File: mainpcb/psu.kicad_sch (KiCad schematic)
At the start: 16 parts, among them J2 8PCV-06-006, U3 LM2576T-5

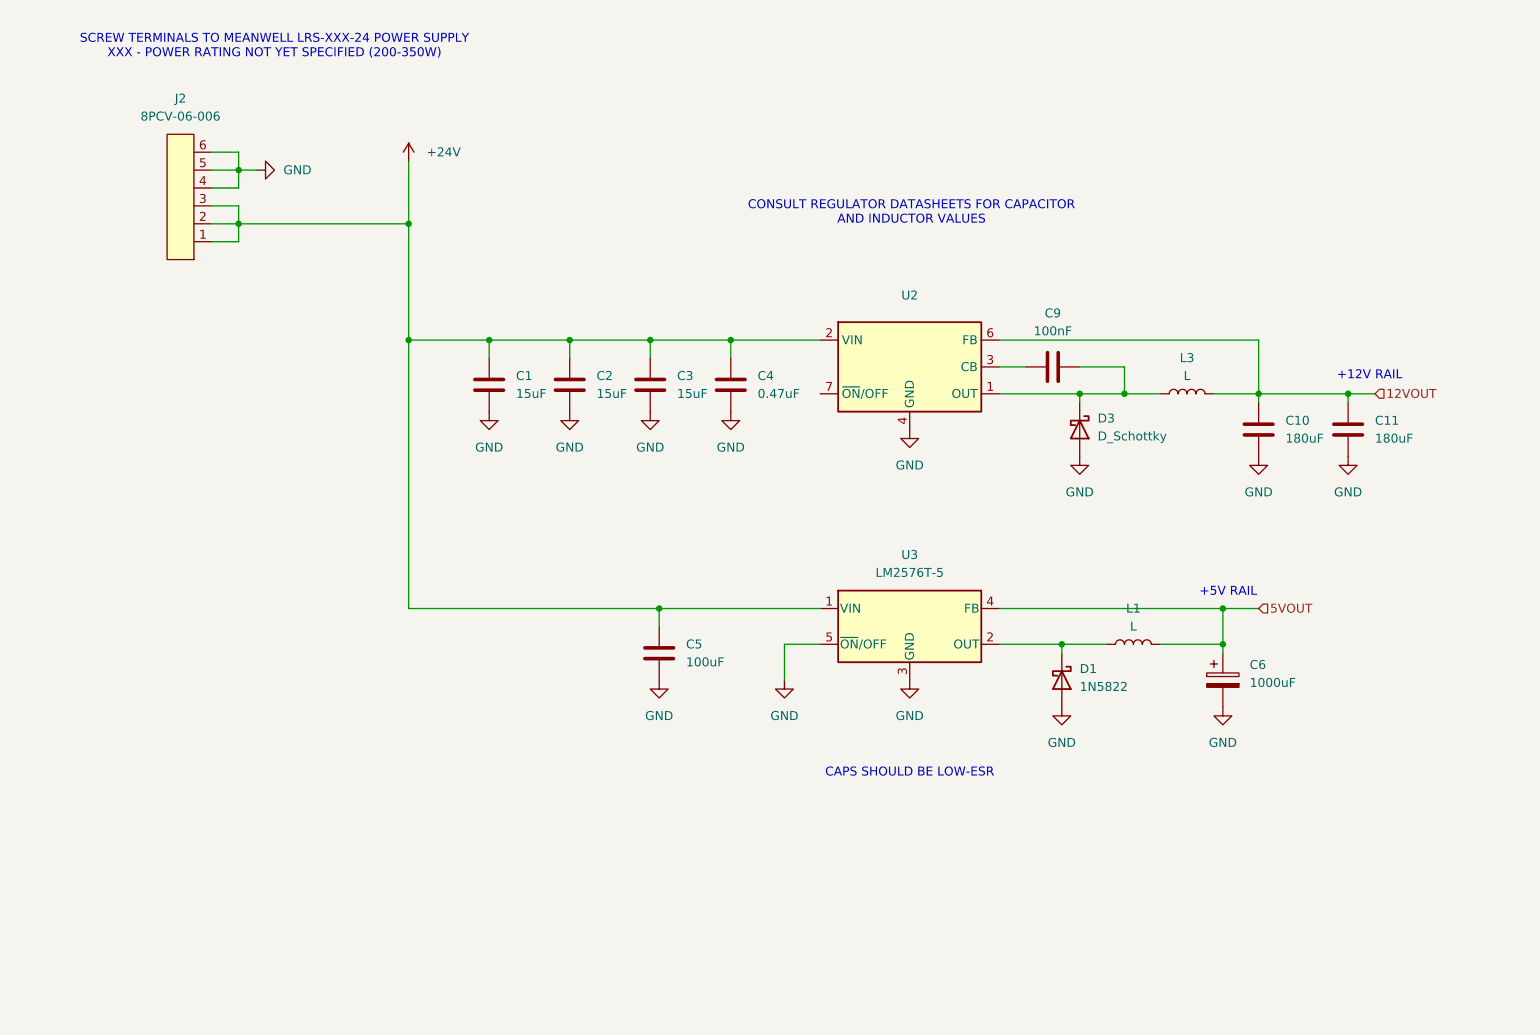
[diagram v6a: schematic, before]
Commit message: Added limit switches to hand and readme
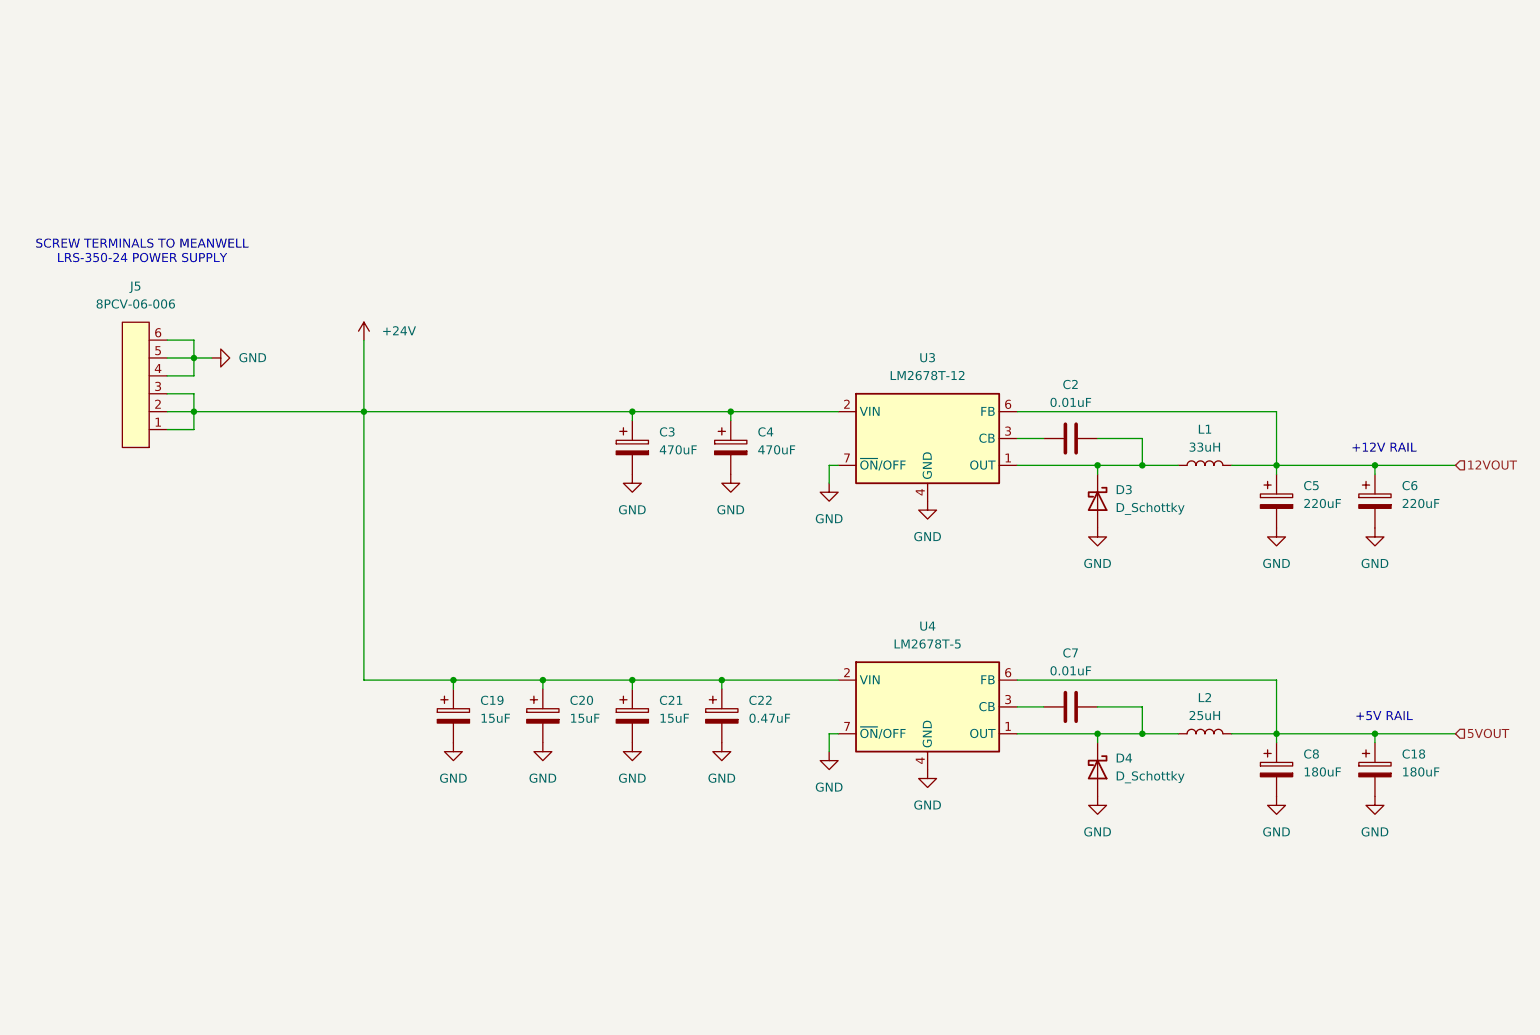
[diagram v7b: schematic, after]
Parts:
- removed C1, C2, C3: 15uF, symbol Device:C
- removed C10, C11: 180uF, symbol Device:C
- removed C4: 0.47uF, symbol Device:C
- removed C5: 100uF, symbol Device:C
- removed D1: 1N5822, symbol Device:D_Schottky
- removed L1: L, symbol Device:L
- removed U2: ~, symbol bh_symbol_library:LM2678T-12
- removed U3: LM2576T-5, Package_TO_SOT_THT:TO-220-5_P3.4x3.7mm_StaggerOdd_Lead3.8mm_Vertical, symbol Regulator_Switching:LM2576T-5
- added C18, C8: 180uF, Capacitor_THT:CP_Radial_D16.0mm_P7.50mm, symbol Device:C_Polarized
- added C19, C20, C21: 15uF, Capacitor_THT:CP_Radial_D12.5mm_P5.00mm, symbol Device:C_Polarized
- added C22: 0.47uF, Capacitor_THT:CP_Radial_D5.0mm_P2.50mm, symbol Device:C_Polarized
- added C3, C4: 470uF, Capacitor_THT:CP_Radial_D10.0mm_P5.00mm, symbol Device:C_Polarized
- added C5: 220uF, Capacitor_THT:CP_Radial_D12.5mm_P5.00mm, symbol Device:C_Polarized
- added C7: 0.01uF, Capacitor_THT:C_Rect_L4.0mm_W2.5mm_P2.50mm, symbol Device:C
- added D4: D_Schottky, Diode_THT:D_DO-27_P15.24mm_Horizontal, symbol Device:D_Schottky
- added L2: 25uH, Inductor_THT:L_Toroid_Vertical_L16.5mm_W11.4mm_P7.62mm_Pulse_KM-2, symbol Device:L
- added U3: LM2678T-12, Package_TO_SOT_THT:TO-220-7_P2.54x3.7mm_StaggerOdd_Lead3.8mm_Vertical, symbol bh_symbol_library:LM2678T-12
- added U4: LM2678T-5, Package_TO_SOT_THT:TO-220-7_P2.54x3.7mm_StaggerOdd_Lead3.8mm_Vertical, symbol bh_symbol_library:LM2687T-5
- C2: renamed from C9; value 100nF -> 0.01uF; footprint (none) -> Capacitor_THT:C_Rect_L4.0mm_W2.5mm_P2.50mm
- C6: value 1000uF -> 220uF; footprint (none) -> Capacitor_THT:CP_Radial_D12.5mm_P5.00mm; Digikey (none) -> https://www.digikey.ca/en/products/detail/nichicon/UHW2A221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
- D3: footprint Package_TO_SOT_SMD:TO-263-2 -> Diode_THT:D_DO-27_P15.24mm_Horizontal; Digikey (none) -> https://www.digikey.ca/en/products/detail/onsemi/80SQ045NRL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
- L1: renamed from L3; value L -> 33uH; footprint (none) -> Inductor_THT:L_Toroid_Vertical_L24.6mm_W15.5mm_P11.44mm_Pulse_KM-4; Digikey (none) -> https://www.digikey.ca/en/products/detail/pulse-electronics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
- renumbered J2 to J5
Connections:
- net +24V: now also C19.1, C20.1, C21.1, C22.1, C3.1, C4.1, U3.2 (VIN), U4.2 (VIN)
- net 12VOUT: now also C6.1, C5.1, U3.6 (FB)
- net 5VOUT: now also C18.1, C8.1, L2.2, U4.6 (FB); no longer C6.1
- net GND: now also C18.2, C19.2, C20.2, C21.2, C22.2, C3.2, C4.2, C5.2, C8.2, D4.2 (A), U3.4 (GND), U3.7 (~{ON}/OFF), U4.4 (GND), U4.7 (~{ON}/OFF)
- net at C2.2, D3.1 (K), L1.1: now also U3.1 (OUT)
- net at C2.1: now also U3.3 (CB)
- new net: C7.2, D4.1 (K), L2.1, U4.1 (OUT)
- new net: C7.1, U4.3 (CB)
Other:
- note added: "SCREW TERMINALS TO MEANWELL LRS-350-24 POWER SUPPLY"
- note removed: "CAPS SHOULD BE LOW-ESR"
- note removed: "CONSULT REGULATOR DATASHEETS FOR CAPACITOR AND INDUCTOR VALUES"
- note removed: "SCREW TERMINALS TO MEANWELL LRS-XXX-24 POWER SUPPLY XXX - POWER RATING NOT YET SPECIFIED (200-350W)"
- moved on the sheet: C2, D3, J5, L1

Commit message: Started layout of control board
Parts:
- removed C19, C20, C21: 15uF, Capacitor_THT:CP_Radial_D12.5mm_P5.00mm, symbol Device:C_Polarized
- removed C22: 0.47uF, Capacitor_THT:CP_Radial_D5.0mm_P2.50mm, symbol Device:C_Polarized
- removed C4: 470uF, Capacitor_THT:CP_Radial_D10.0mm_P5.00mm, symbol Device:C_Polarized
- removed C8: 180uF, Capacitor_THT:CP_Radial_D16.0mm_P7.50mm, symbol Device:C_Polarized
- added C4, C8: 0.1uF, Capacitor_THT:C_Rect_L4.0mm_W2.5mm_P2.50mm, symbol Device:C
- C18: value 180uF -> 330uF; footprint Capacitor_THT:CP_Radial_D16.0mm_P7.50mm -> Capacitor_THT:C_Radial_D10.0mm_H12.5mm_P5.00mm; Digikey https://www.digikey.ca/en/products/detail/nichicon/UCY2C181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 -> https://www.digikey.ca/en/products/detail/panasonic-electro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
- C3: value 470uF -> 82uF; footprint Capacitor_THT:CP_Radial_D10.0mm_P5.00mm -> Capacitor_THT:CP_Radial_D8.0mm_P3.50mm; Digikey https://www.digikey.ca/en/products/detail/nichicon/UHW1H471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 -> https://www.digikey.ca/en/products/detail/panasonic-electro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
- C5: value 220uF -> 180uF; footprint Capacitor_THT:CP_Radial_D12.5mm_P5.00mm -> Capacitor_THT:CP_Radial_D8.0mm_P3.50mm; Digikey https://www.digikey.ca/en/products/detail/nichicon/UHW2A221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 -> https://www.digikey.ca/en/products/detail/panasonic-electro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
- C6: value 220uF -> 39uF; footprint Capacitor_THT:CP_Radial_D12.5mm_P5.00mm -> Capacitor_THT:CP_Radial_D8.0mm_P3.50mm; Digikey https://www.digikey.ca/en/products/detail/nichicon/UHW2A221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 -> https://www.digikey.ca/en/products/detail/panasonic-electro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
- J5: footprint (none) -> bh_footprint_library:Terminal_Block_8PCV-06-006
- L1: footprint Inductor_THT:L_Toroid_Vertical_L24.6mm_W15.5mm_P11.44mm_Pulse_KM-4 -> Inductor_THT:L_Toroid_Vertical_L31.8mm_W15.9mm_P13.50mm_Bourns_5700; Digikey https://www.digikey.ca/en/products/detail/pulse-electronics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 -> https://www.digikey.ca/en/products/detail/signal-transforme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; OldDigikey (none) -> https://www.digikey.ca/en/products/detail/pulse-electronics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
- L2: value 25uH -> 15uH; footprint Inductor_THT:L_Toroid_Vertical_L16.5mm_W11.4mm_P7.62mm_Pulse_KM-2 -> Inductor_THT:L_Toroid_Vertical_L31.8mm_W15.9mm_P13.50mm_Bourns_5700; Digikey https://www.digikey.ca/en/products/detail/pulse-electronics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 -> https://www.digikey.ca/en/products/detail/signal-transforme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
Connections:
- net +24V: now also C6.1, C4.1, C8.1
- net 12VOUT: no longer C6.1
- net GND: now also C4.2, C8.2
